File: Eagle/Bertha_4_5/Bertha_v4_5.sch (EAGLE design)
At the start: 133 parts, among them CON1 JACK_DC_BARREL, CON2 JACK_DC_BARREL, IC1 MCP1703DB, IC4 DRV8811, J1 RJ12RIGHTANGLE-I2C, J2 RJ12RIGHTANGLE-I2C, Q5 BSP75, Q6 BSP75, U1 HX711, U100 RN2483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

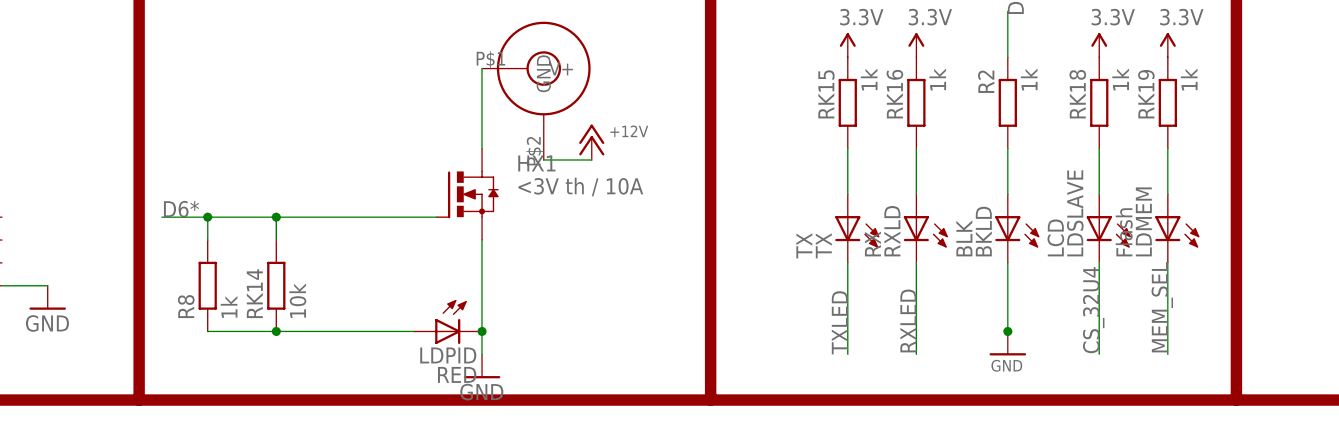
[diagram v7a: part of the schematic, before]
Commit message: Corrected minor mistakes on pull uo/down lines closes #90 , Gebers to be recreated
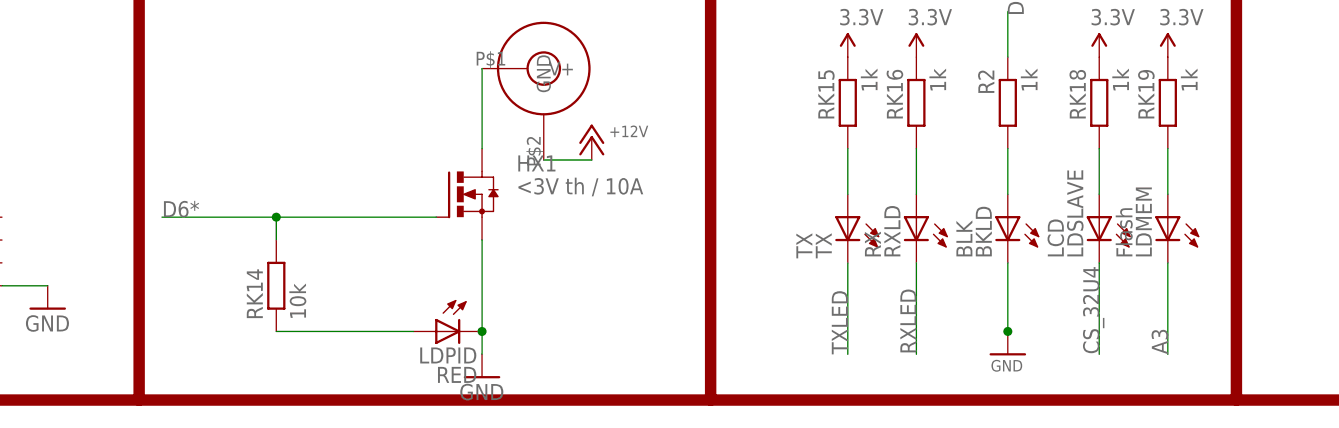
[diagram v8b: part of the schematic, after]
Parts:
- removed R8: 1k, rcl:R-EU_R0805
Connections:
- net A3: now also LDMEM.C
- net D6*: no longer R8.2
- net MEM_SEL: no longer LDMEM.C
- net N$26: no longer R8.1
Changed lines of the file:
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@@
 <?xml version="1.0" encoding="utf-8"?>
 <!DOCTYPE eagle SYSTEM "eagle.dtd">
-<eagle version="7.7.0">
+<eagle version="7.5.0">
 <drawing>
 <settings>
@@
 <part name="JP3" library="jumper" deviceset="JP4E" device=""/>
 <part name="R4" library="rcl" deviceset="R-EU_" device="R0805" value="100"/>
-<part name="R8" library="rcl" deviceset="R-EU_" device="R0805" value="1k"/>
 </parts>
 <sheets>
@@
 <instance part="JP3" gate="G$1" x="350.52" y="127" rot="R270"/>
 <instance part="R4" gate="G$1" x="279.4" y="53.34" rot="MR90"/>
-<instance part="R8" gate="G$1" x="330.2" y="20.32" rot="R90"/>
 </instances>
 <busses>
@@
 <label x="396.24" y="254" size="1.778" layer="95"/>
 </segment>
+<segment>
+<pinref part="LDMEM" gate="G$1" pin="C"/>
+<wire x1="436.88" y1="22.86" x2="436.88" y2="12.7" width="0.1524" layer="91"/>
+<label x="436.88" y="12.7" size="1.778" layer="95" rot="R90"/>
+</segment>
 </net>
 <net name="A4" class="0">
@@
 <segment>
 <pinref part="HX1" gate="G$1" pin="G"/>
-<wire x1="325.12" y1="27.94" x2="330.2" y2="27.94" width="0.1524" layer="91"/>
-<wire x1="330.2" y1="27.94" x2="337.82" y2="27.94" width="0.1524" layer="91"/>
+<wire x1="325.12" y1="27.94" x2="337.82" y2="27.94" width="0.1524" layer="91"/>
 <wire x1="337.82" y1="27.94" x2="337.82" y2="25.4" width="0.1524" layer="91"/>
 <junction x="337.82" y="27.94"/>
@@
 <wire x1="355.6" y1="27.94" x2="337.82" y2="27.94" width="0.1524" layer="91"/>
 <label x="325.12" y="27.94" size="1.778" layer="95"/>
-<pinref part="R8" gate="G$1" pin="2"/>
-<wire x1="330.2" y1="25.4" x2="330.2" y2="27.94" width="0.1524" layer="91"/>
-<junction x="330.2" y="27.94"/>
 </segment>
 </net>
@@
 <wire x1="353.06" y1="15.24" x2="337.82" y2="15.24" width="0.1524" layer="91"/>
 <pinref part="LDPID" gate="G$1" pin="A"/>
-<pinref part="R8" gate="G$1" pin="1"/>
-<wire x1="330.2" y1="15.24" x2="337.82" y2="15.24" width="0.1524" layer="91"/>
-<junction x="337.82" y="15.24"/>
 </segment>
 </net>
@@
 <net name="MEM_SEL" class="0">
 <segment>
-<pinref part="LDMEM" gate="G$1" pin="C"/>
-<wire x1="436.88" y1="22.86" x2="436.88" y2="12.7" width="0.1524" layer="91"/>
-<label x="436.88" y="12.7" size="1.778" layer="95" rot="R90"/>
-</segment>
-<segment>
 <wire x1="421.64" y1="251.46" x2="414.02" y2="251.46" width="0.1524" layer="91"/>
